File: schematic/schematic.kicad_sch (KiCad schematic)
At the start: 14 parts, among them J1 Conn_01x06, U1 ATmega328-PU

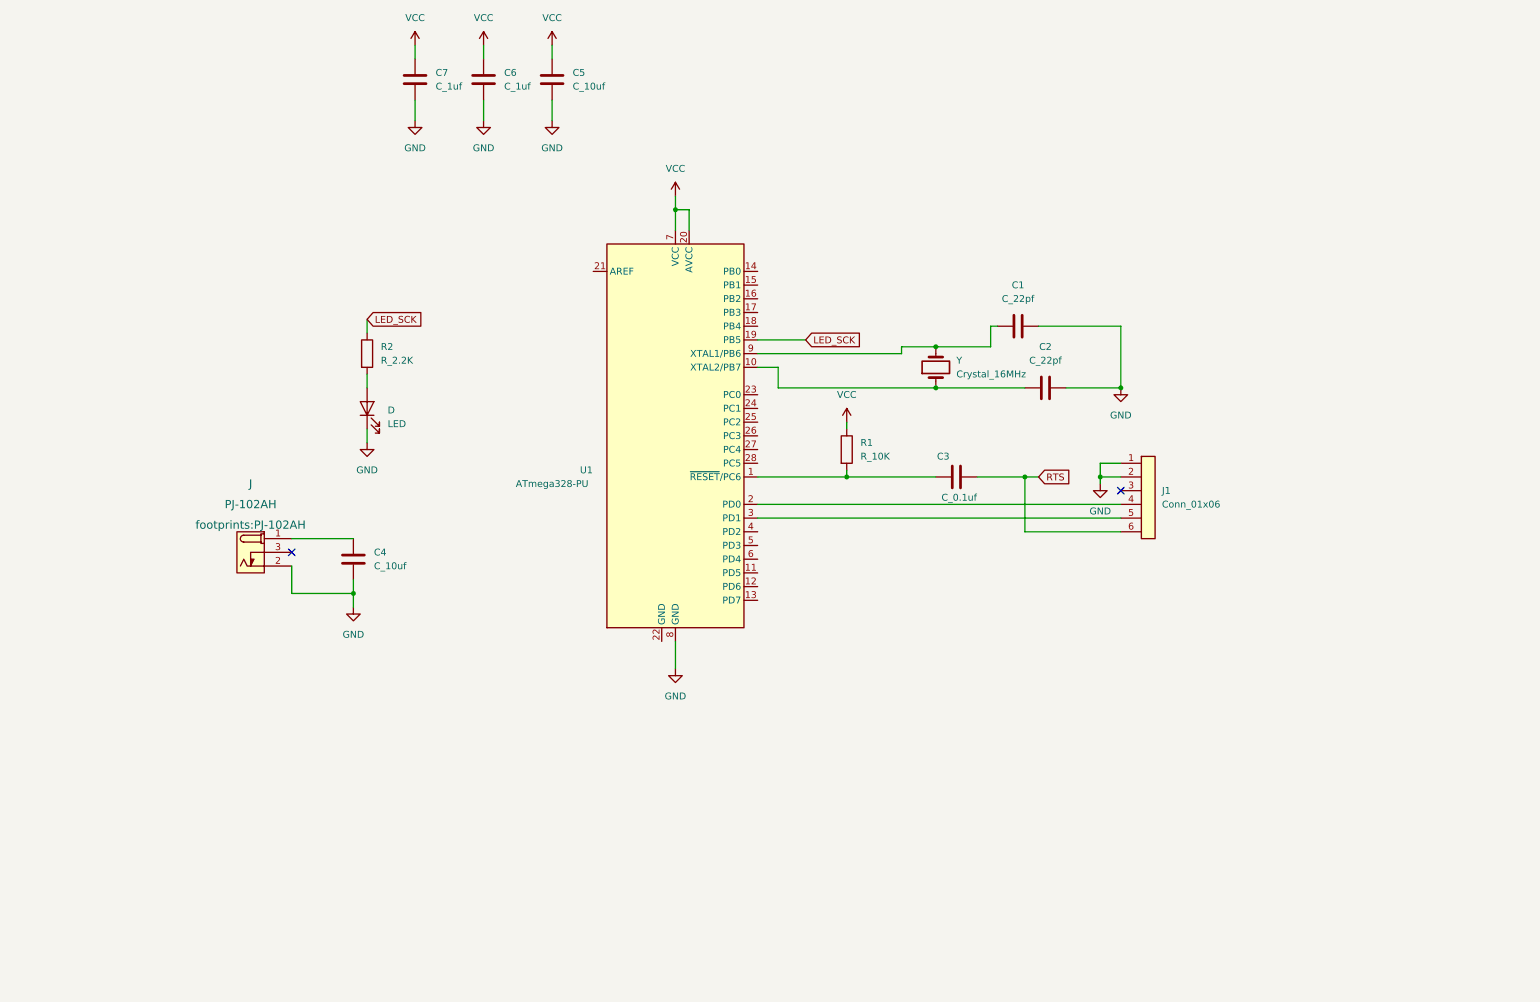
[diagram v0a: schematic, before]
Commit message: updated schematic with battery connections and reset button
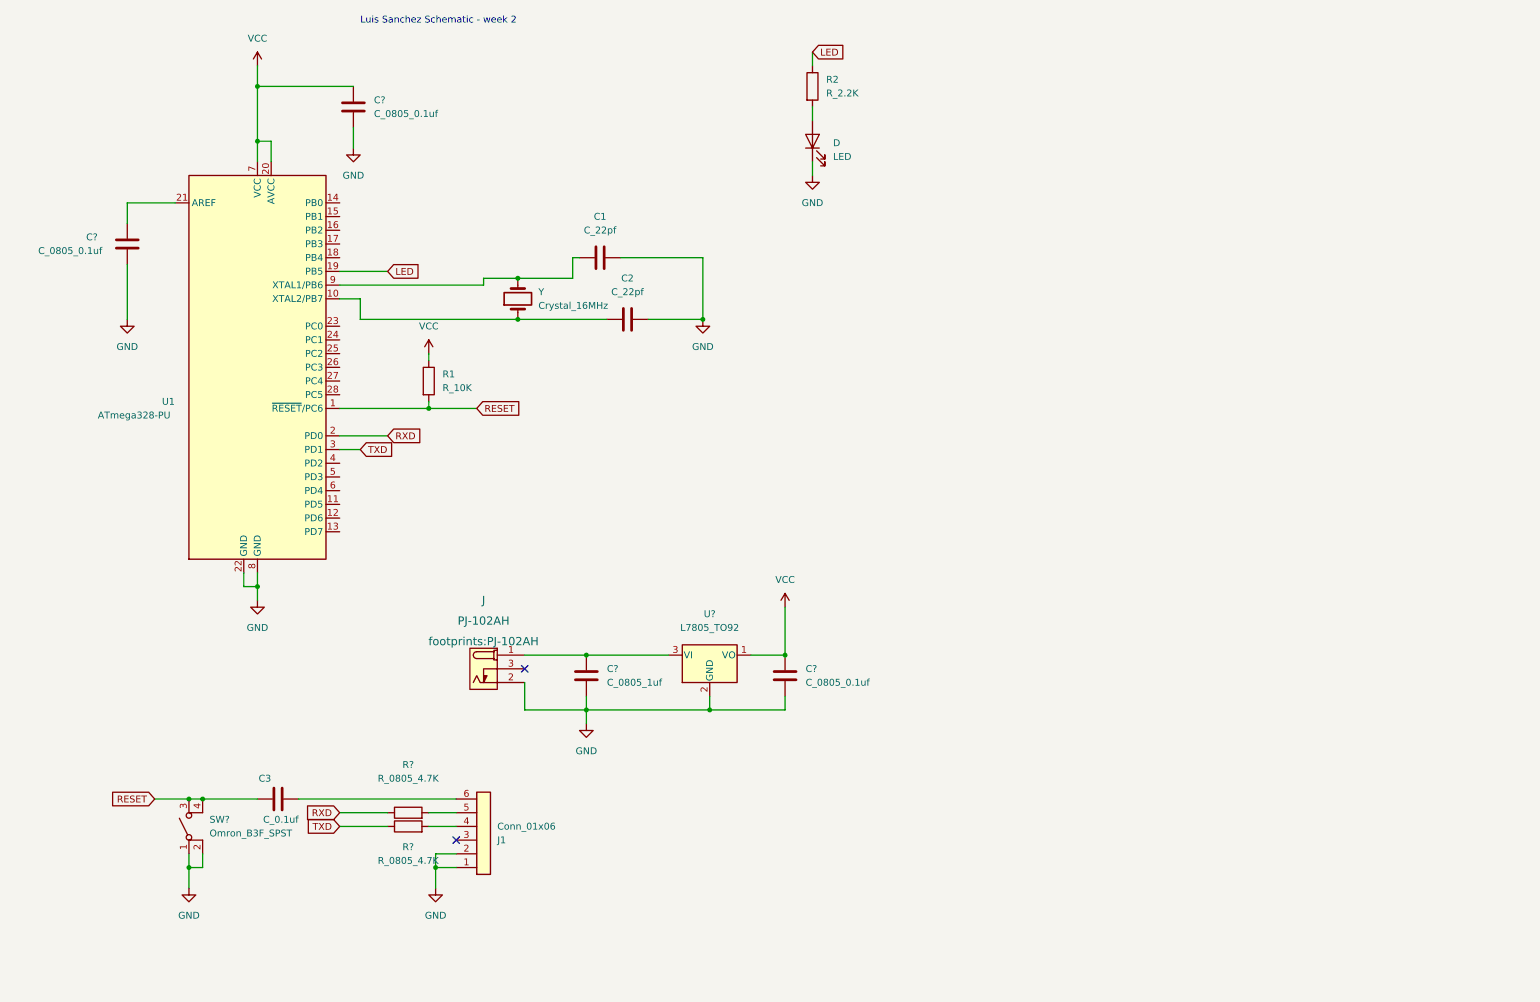
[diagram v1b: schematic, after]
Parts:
- removed C4, C5: C_10uf, footprints:C_0805_2012Metric, symbol HPS:C_0805_10uf
- removed C6, C7: C_1uf, footprints:C_0805_2012Metric, symbol HPS:C_0805_1uf
- added C?: C_0805_1uf, footprints:C_0805_2012Metric, symbol HPS:C_0805_1uf
- added C? (x3): C_0805_0.1uf, footprints:C_0805_2012Metric, symbol HPS:C_0805_0.1uf
- added R? (x2): R_0805_4.7K, footprints:R_0805_2012Metric, symbol HPS:R_0805_4.7K
- added SW?: Omron_B3F_SPST, footprints:SW_SPST_Omron_B3FS-100xP, symbol HPS:Omron_B3F_SPST
- added U?: L7805_TO92, footprints:TO-92_Inline, symbol HPS:L7805_TO92
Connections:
- net GND: now also U1.22 (GND), C?.2, C?.2, C?.2, C?.2, SW?.1 (A), SW?.2 (A), U?.2 (GND)
- net VCC: now also C?.1, C?.1, U?.1 (VO)
- net at J.1 (POLE): now also C?.1, U?.3 (VI)
- net RESET: now reaches C3.1, R1.2, U1.1 (~{RESET}/PC6)
- net RESET: now also SW?.3 (B), SW?.4 (B)
- net at J1.4 (Pin_4): now also R?.2; no longer U1.2 (PD0)
- net at U1.21 (AREF): now also C?.1
- net at J1.5 (Pin_5): now also R?.2; no longer U1.3 (PD1)
- net LED_SCK renamed LED
- net RTS: no longer names the net of C3.2, J1.6 (Pin_6)
- new net RXD: R?.1, U1.2 (PD0)
- new net TXD: R?.1, U1.3 (PD1)
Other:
- note added: "Luis Sanchez Schematic - week 2"
- moved on the sheet: C1, C2, C3, D, J, J1, R1, R2, U1, Y

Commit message: week 3 updates
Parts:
- added DS?: LED_Display_1001, footprints:Adafruit-1001-0-0-MFG, symbol HPS:LED_Display_1001
- added R?: R_0805_10K, footprints:R_0805_2012Metric, symbol HPS:R_0805_10K
- added R? (x3): R_0805_1K, footprints:R_0805_2012Metric, symbol HPS:R_0805_1K
- added SW2, SW3, SW4: Omron_B3F_SPST, footprints:SW_SPST_Omron_B3FS-100xP, symbol HPS:Omron_B3F_SPST
- added U2: DS1307_DIP-8, footprints:DIP-8_W7.62mm, symbol HPS:DS1307_DIP-8
- added U?: MAX7219, footprints:DIP-24_W7.62mm, symbol HPS:MAX7219
- added Y2: Crystal_32768Hz, footprints:Crystal_SMD_2Pin_3.2x1.5mm, symbol HPS:Crystal_32768Hz
- gave numbers to parts that had none: 1
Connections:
- net GND: now also U1.23 (PC0), U1.24 (PC1), U1.25 (PC2), SW2.3 (B), SW3.3 (B), SW4.3 (B), U2.4 (GND), U?.4 (GND), U?.9 (GND)
- net LED: now also U1.4 (PD2); no longer U1.19 (PB5)
- net VCC: now also R?.1, R?.1, R?.1, R?.2, U2.8 (VCC), U?.19 (V+)
- net Din: now reaches U1.16 (PB2)
- net Din: now also U?.1 (DIN)
- net CS: now reaches U1.17 (PB3)
- net CS: now also U?.12 (LOAD)
- net PHR: now reaches U1.26 (PC3)
- net SDA: now reaches U1.27 (PC4)
- net SDA: now also U2.5 (SDA)
- net SCL: now reaches U1.28 (PC5)
- net SCL: now also U2.6 (SCL)
- new net: R?.2, SW4.1 (A)
- new net: R?.2, SW2.1 (A)
- new net: R?.2, SW3.1 (A)
- new net: U2.1 (X1), Y2.1
- new net: U2.2 (X2), Y2.2
- new net: R?.1, U?.18 (ISET)
- new net: DS?.9 (B), U?.11 (DIG_1)
- new net: DS?.11 (COM_DIG.2), U?.14 (SEG_A)
- new net: DS?.10 (COM_DIG.3), U?.15 (SEG_F)
- new net: DS?.7 (COM_COLON), U?.16 (SEG_B)
- new net: DS?.5 (G), U?.17 (SEG_G)
- new net: DS?.12 (F), U?.2 (DIG_0)
- new net: DS?.4 (C), U?.20 (SEG_C)
- new net: DS?.1 (E), U?.21 (SEG_E)
- new net: DS?.3 (DP), U?.22 (SEG_DP)
- new net: DS?.2 (D), U?.23 (SEG_D)
- new net: DS?.8 (COLON), U?.6 (DIG_2)
- new net: DS?.6 (COM_DIG.4), U?.7 (DIG_3)
- new net +BATT: U2.3 (VBAT)
- new net SCK: U1.19 (PB5), U?.13 (CLK)
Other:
- moved on the sheet: C3, C?, D, J, J1, R2, R?, SW1, U?

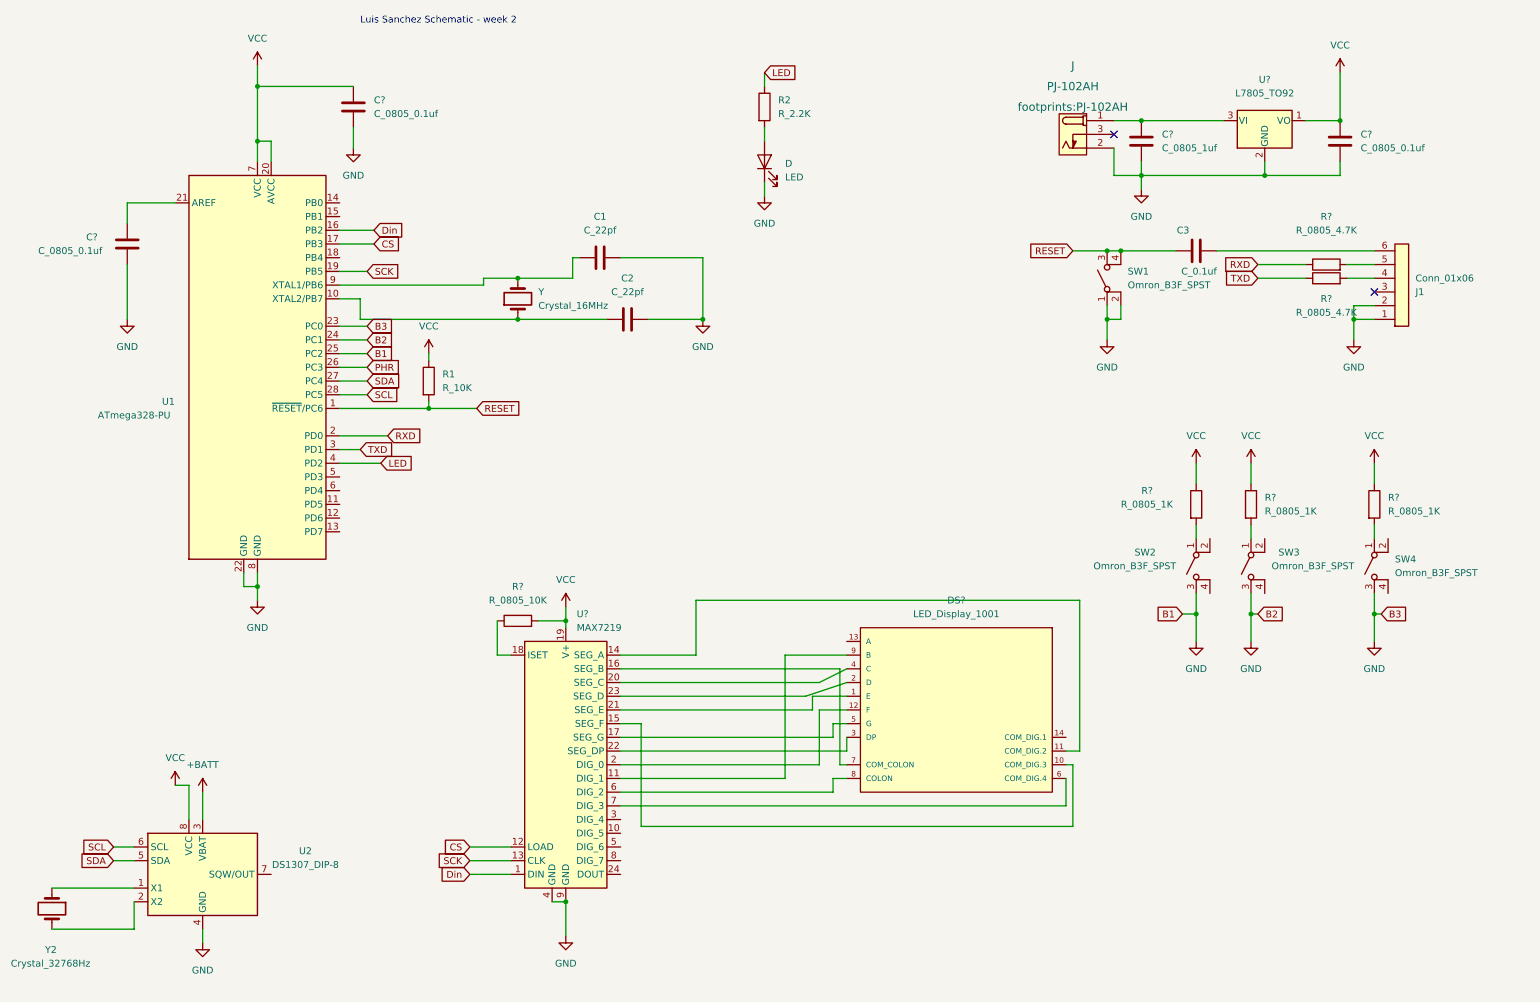
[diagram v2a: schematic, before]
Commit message: Moved schematic to rectangle template
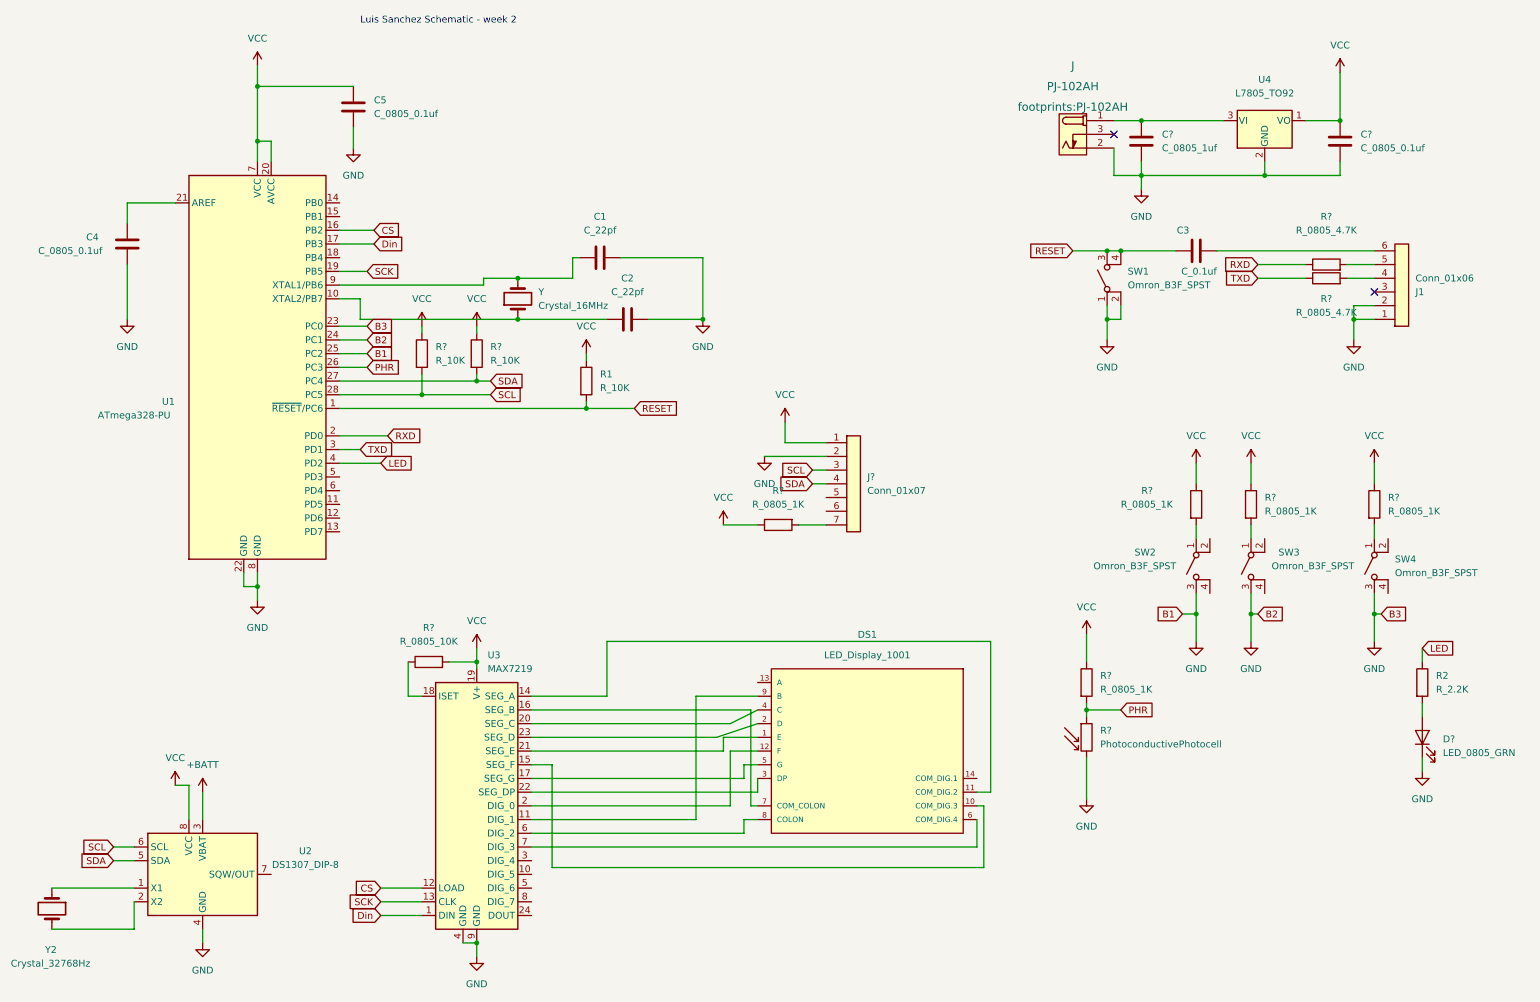
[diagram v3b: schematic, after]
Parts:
- removed D: LED, footprints:LED_0805_2012Metric, symbol HPS:LED_0805
- added D?: LED_0805_GRN, footprints:LED_0805_2012Metric, symbol HPS:LED_0805_GRN
- added J?: Conn_01x07, footprints:PinHeader_1x07_P2.54mm_Vertical, symbol HPS:Conn_01x07
- added R? (x2): R_0805_1K, footprints:R_0805_2012Metric, symbol HPS:R_0805_1K
- added R? (x2): R_10K, footprints:R_0805_2012Metric, symbol HPS:R_0805_10K
- added R?: PhotoconductivePhotocell, footprints:R_LDR_4.9x4.2mm_P2.54mm_Vertical, symbol HPS:PhotoconductivePhotocell
- gave numbers to parts that had none: 5
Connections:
- net CS: now also U1.16 (PB2); no longer U1.17 (PB3)
- net Din: now also U1.17 (PB3); no longer U1.16 (PB2)
- net GND: now also D?.1 (K), J?.2 (Pin_2), R?.2
- net PHR: now also R?.1, R?.2
- net SCL: now also J?.3 (Pin_3), R?.2
- net SDA: now also J?.4 (Pin_4), R?.2
- net VCC: now also J?.1 (Pin_1), R?.1, R?.1, R?.1, R?.1
- net at R2.2: now also D?.2 (A)
- new net: J?.7 (Pin_7), R?.2
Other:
- moved on the sheet: DS1, R1, R2, R?, U3
